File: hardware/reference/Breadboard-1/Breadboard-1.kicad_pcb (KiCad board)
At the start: 2 copper layers, 50.8 x 69.9 mm, 60 parts, among them J1 Left, J2 Right, J3 ICSP, J4 TTL Serial, Q31 HSM0903, Q32 HSM0903, Q41 2N7002, Q42 2N7002, Q43 2N7002, U11 AMS1117-5.0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

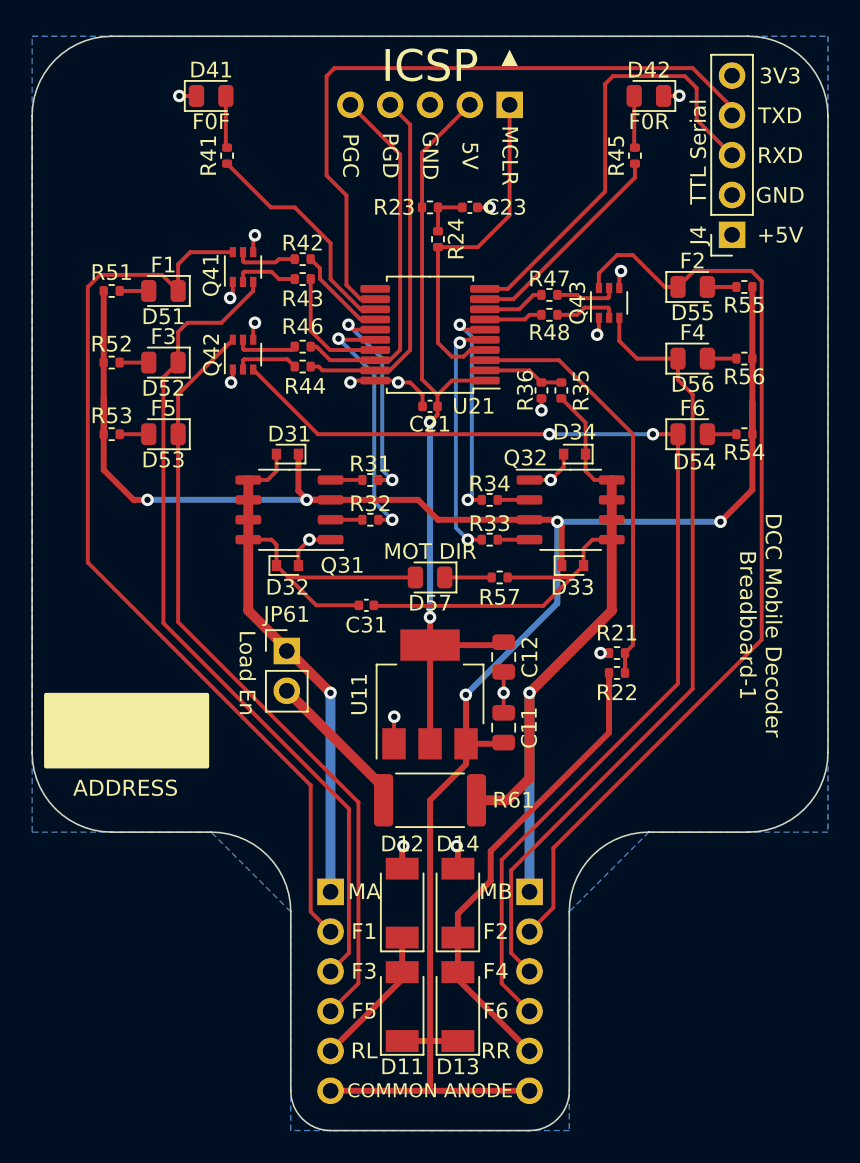
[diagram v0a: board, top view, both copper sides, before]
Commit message: Add pre-biased transistors to drive high side.  Update LED part to more common.
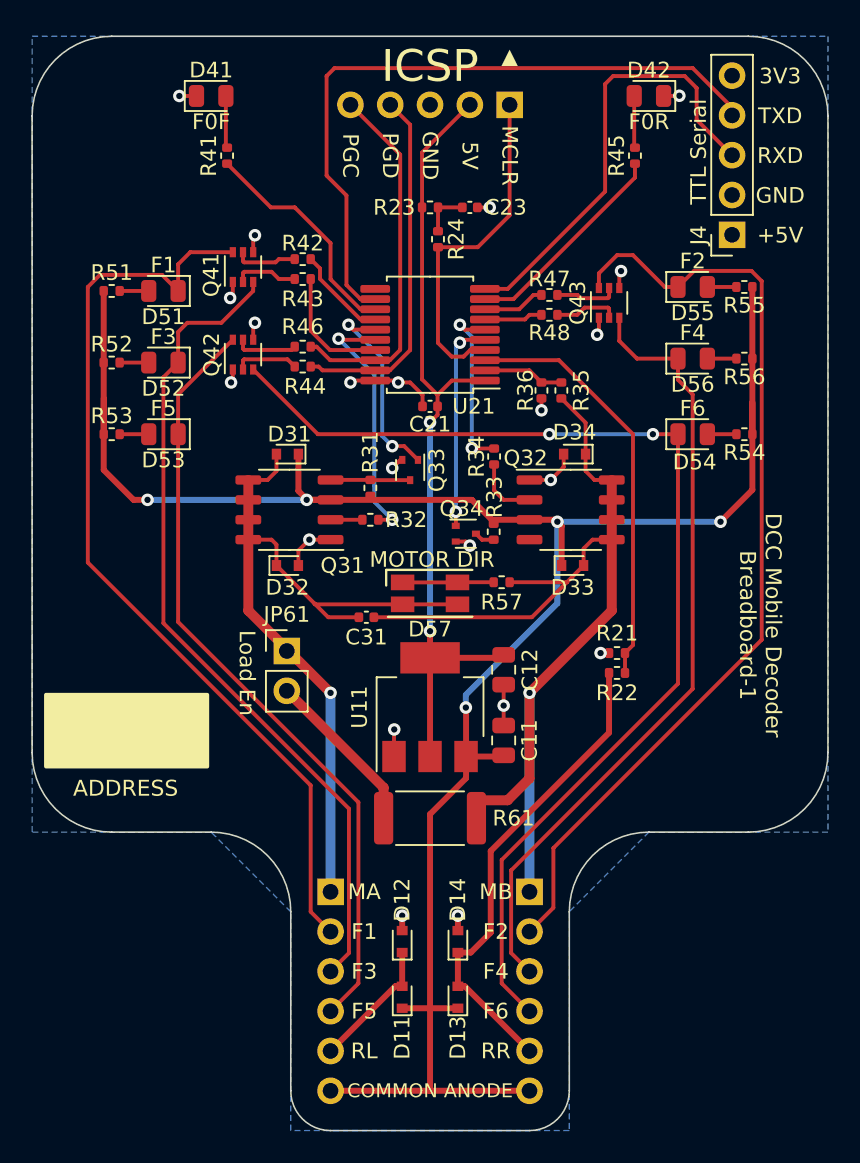
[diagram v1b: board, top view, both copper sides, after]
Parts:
- added Q33: DTC143ZE, Package_TO_SOT_SMD:SOT-523, F.Cu at (74.9, 78.5)
- added Q34: DTC143ZE, Package_TO_SOT_SMD:SOT-523, F.Cu at (78.5, 82.5)
- D11, D12, D13, D14: footprint Diode_SMD:D_SOD-128 -> Diode_SMD:D_SOD-523
- D57: value MOT DIR -> MOTOR DIR; footprint LED_SMD:LED_0805_2012Metric -> LED_SMD:LED_RGB_1210
- R31, R33: value 220 -> 10K
- moved R34 2.78 mm to (80.3, 77.6), turned to 90 degrees
- moved D12 2.45 mm to (74.4, 108.6)
- moved D14 2.45 mm to (78.0, 108.6)
- moved R61 1.14 mm to (76.2, 100.7)
- moved D57 1.02 mm to (76.2, 86.4), turned to 0 degrees
- moved C11 0.81 mm to (80.9, 95.7)
- moved C12 0.81 mm to (80.9, 91.2)
- moved U11 0.81 mm to (76.2, 93.6)
- moved C31 0.76 mm to (72.1, 87.9)
- moved D11 0.59 mm to (74.4, 112.1)
- moved D13 0.59 mm to (78.0, 112.1)
- moved R33 0.57 mm to (80.3, 82.4), turned to 90 degrees
- moved R31 0.51 mm to (72.4, 79.6), turned to -90 degrees
- moved R57 0.33 mm to (80.8, 85.6)
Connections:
- R31 pad 1: P1A -> Net-(Q31-Pad4)
- R31 pad 2: Net-(Q31-Pad4) -> Vdrive
- R33 pad 2: P1C -> Vdrive
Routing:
- net Net-(Q31-Pad4): track 2.03 -> 5.09 mm
- net P1D: track 14.2 -> 11.3 mm
- net Net-(D57-Pad1): track 3.00 -> 5.82 mm
- net Net-(Q32-Pad2): track 2.03 -> 4.16 mm
- net P1C: track 15.6 -> 13.5 mm
- net MOT_A: track 49.3 -> 50.6 mm
- net Net-(JP61-Pad2): track 9.55 -> 10.7 mm
- net GND: track 30.4 -> 31.4 mm, vias 19 -> 21
- net P1A: track 13.8 -> 12.7 mm
- net +5V: track 50.8 -> 51.6 mm
- net RAIL_R: track 30.4 -> 31.1 mm
- net Net-(Q32-Pad4): track 2.03 -> 1.29 mm
- net RAIL_L: track 9.46 -> 8.77 mm

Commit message: Attempt to refactor with all SOT-23 components for cost, availability.
Also makes it more possible to hand-solder.
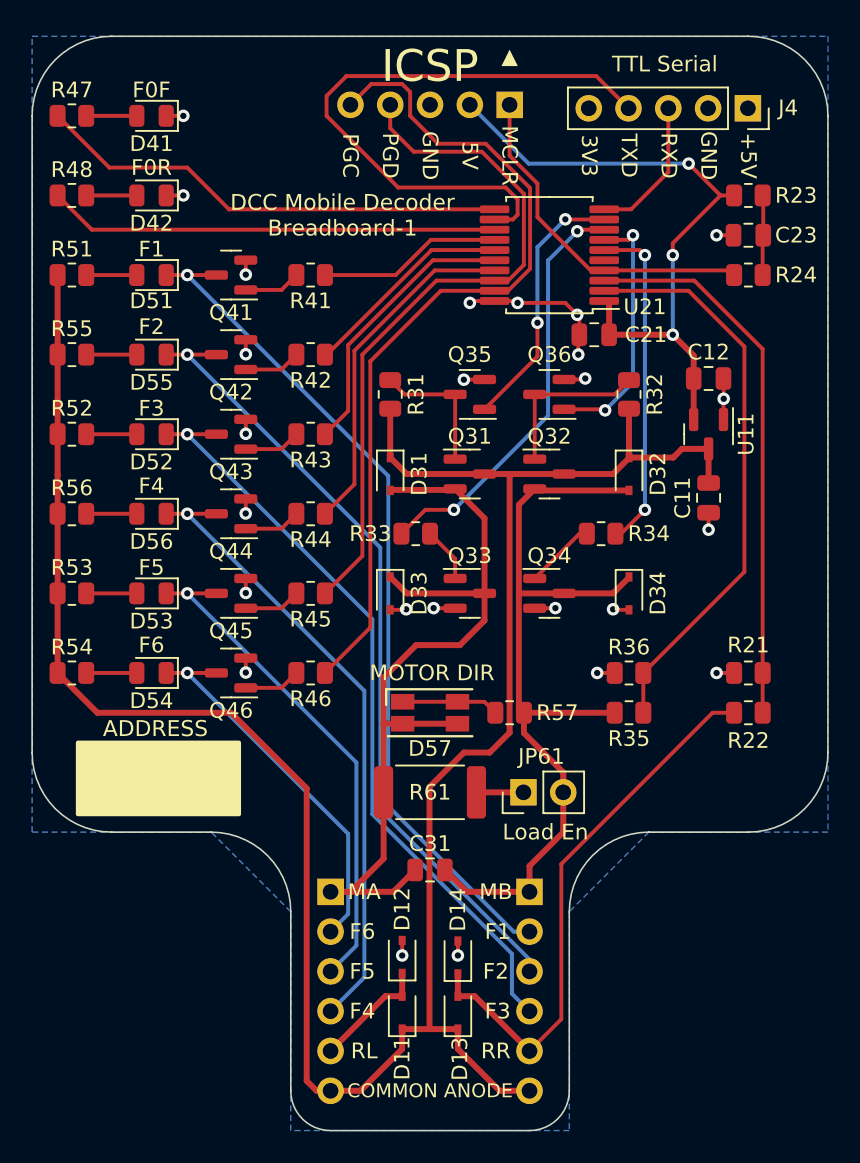
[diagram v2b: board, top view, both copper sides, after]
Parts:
- added Q33: DMN6140L-7, Package_TO_SOT_SMD:SOT-23, F.Cu at (78.7, 86.4)
- added Q34: DMN6140L-7, Package_TO_SOT_SMD:SOT-23, F.Cu at (83.8, 86.4)
- added Q44: 2N7002K, Package_TO_SOT_SMD:SOT-23, F.Cu at (63.5, 81.3)
- added Q45: 2N7002K, Package_TO_SOT_SMD:SOT-23, F.Cu at (63.5, 86.4)
- added Q46: 2N7002K, Package_TO_SOT_SMD:SOT-23, F.Cu at (63.5, 91.4)
- C21, C23, C31: footprint Capacitor_SMD:C_0402_1005Metric -> Capacitor_SMD:C_0805_2012Metric
- D11, D12, D13, D14, D31, D34: footprint Diode_SMD:D_SOD-523 -> Diode_SMD:D_SOD-323
- D32: renamed from D33; footprint Diode_SMD:D_SOD-523 -> Diode_SMD:D_SOD-323
- D33: renamed from D32; footprint Diode_SMD:D_SOD-523 -> Diode_SMD:D_SOD-323
- Q31, Q32: value HSM0903 -> NCE2309; footprint Package_SO:SOP-8_3.9x4.9mm_P1.27mm -> Package_TO_SOT_SMD:SOT-23
- Q35: renamed from Q33; value DTC143ZE -> DTC143ZCA; footprint Package_TO_SOT_SMD:SOT-523 -> Package_TO_SOT_SMD:SOT-23
- Q36: renamed from Q34; value DTC143ZE -> DTC143ZCA; footprint Package_TO_SOT_SMD:SOT-523 -> Package_TO_SOT_SMD:SOT-23
- Q41, Q42, Q43: value 2N7002 -> 2N7002K; footprint Package_TO_SOT_SMD:SOT-363_SC-70-6 -> Package_TO_SOT_SMD:SOT-23
- R21, R22, R23, R24, R31, R34, R35, R36, R43, R46, R51, R52, R53, R54, R55, R56, R57: footprint Resistor_SMD:R_0402_1005Metric -> Resistor_SMD:R_0805_2012Metric
- R32: renamed from R33; footprint Resistor_SMD:R_0402_1005Metric -> Resistor_SMD:R_0805_2012Metric
- R33: renamed from R32; footprint Resistor_SMD:R_0402_1005Metric -> Resistor_SMD:R_0805_2012Metric
- R41: renamed from R42; footprint Resistor_SMD:R_0402_1005Metric -> Resistor_SMD:R_0805_2012Metric
- R42: renamed from R47; footprint Resistor_SMD:R_0402_1005Metric -> Resistor_SMD:R_0805_2012Metric
- R44: renamed from R48; footprint Resistor_SMD:R_0402_1005Metric -> Resistor_SMD:R_0805_2012Metric
- R45: renamed from R44; footprint Resistor_SMD:R_0402_1005Metric -> Resistor_SMD:R_0805_2012Metric
- R47: renamed from R41; footprint Resistor_SMD:R_0402_1005Metric -> Resistor_SMD:R_0805_2012Metric
- R48: renamed from R45; footprint Resistor_SMD:R_0402_1005Metric -> Resistor_SMD:R_0805_2012Metric
- U11: value AMS1117-5.0 -> ME6203A50M3G; footprint Package_TO_SOT_SMD:SOT-223-3_TabPin2 -> Package_TO_SOT_SMD:SOT-23
- moved R54 45.6 mm to (53.3, 91.4), turned to 0 degrees
- moved R56 44.1 mm to (53.3, 81.3), turned to 0 degrees
- moved R55 43.1 mm to (53.3, 71.1), turned to 0 degrees
- moved D54 37.8 mm to (58.4, 91.4), turned to 180 degrees
- moved R48 36.0 mm to (53.3, 61.0), turned to 0 degrees
- moved D56 35.9 mm to (58.4, 81.3), turned to 180 degrees
- moved D55 34.8 mm to (58.4, 71.1), turned to 180 degrees
- moved D42 32.4 mm to (58.4, 61.0)
- moved Q43 25.5 mm to (63.5, 76.2), turned to 180 degrees
- moved U11 24.9 mm to (94.0, 76.2), turned to -90 degrees
- moved C12 22.7 mm to (94.0, 72.6), turned to 0 degrees
- moved R35 21.0 mm to (88.9, 94.0), turned to 180 degrees
- moved R46 20.8 mm to (68.6, 91.4)
- moved R44 20.7 mm to (68.6, 81.3), turned to 180 degrees
- moved R23 20.3 mm to (96.5, 61.0)
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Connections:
- J1 pad 2: F1_SP -> F6_SP
- J1 pad 3: F3_SP -> F5_SP
- J1 pad 4: F5_SP -> F4_SP
- J2 pad 2: F2_SP -> F1_SP
- J2 pad 3: F4_SP -> F2_SP
- J2 pad 4: F6_SP -> F3_SP
- JP61 pad 1: MOT_A -> Net-(JP61-Pad1)
- JP61 pad 2: Net-(JP61-Pad2) -> MOT_B
- Q31 pad 1: GND -> Net-(Q31-Pad1)
- Q31 pad 2: Net-(Q31-Pad2) -> MOT_A
- Q32 pad 1: GND -> Net-(Q32-Pad1)
- Q32 pad 2: Net-(Q32-Pad2) -> MOT_B
- Q35 pad 3: Net-(Q31-Pad4) -> Net-(Q31-Pad1)
- Q36 pad 3: Net-(Q32-Pad4) -> Net-(Q32-Pad1)
- Q41 pad 1: GND -> Net-(Q41-Pad1)
- Q41 pad 2: Net-(Q41-Pad2) -> GND
- Q41 pad 3: F3_SP -> F1_SP
- Q42 pad 1: GND -> Net-(Q42-Pad1)
- Q42 pad 2: Net-(Q42-Pad2) -> GND
- Q42 pad 3: F6_SP -> F2_SP
- Q43 pad 1: GND -> Net-(Q43-Pad1)
- Q43 pad 2: Net-(Q43-Pad2) -> GND
- Q43 pad 3: F4_SP -> F3_SP
- R31 pad 1: Net-(Q31-Pad4) -> Net-(Q31-Pad1)
- R32 pad 1: Net-(Q32-Pad4) -> Net-(Q32-Pad1)
- R33 pad 2: Net-(Q31-Pad2) -> Net-(Q33-Pad1)
- R34 pad 1: Net-(Q32-Pad2) -> Net-(Q34-Pad1)
- R41 pad 2: Net-(Q41-Pad2) -> Net-(Q41-Pad1)
- R42 pad 2: Net-(Q43-Pad2) -> Net-(Q42-Pad1)
- R43 pad 2: Net-(Q41-Pad5) -> Net-(Q43-Pad1)
- R44 pad 2: Net-(Q43-Pad5) -> Net-(Q44-Pad1)
- R45 pad 2: Net-(Q42-Pad2) -> Net-(Q45-Pad1)
- R46 pad 2: Net-(Q42-Pad5) -> Net-(Q46-Pad1)
- R61 pad 1: Net-(JP61-Pad2) -> MOT_A
- R61 pad 2: MOT_B -> Net-(JP61-Pad1)
- U21 pad 11: unconnected-(U21-Pad11) -> F0F
- U21 pad 13: F0F -> F0R
- U21 pad 14: F3 -> F1
- U21 pad 15: P1A -> F2
- U21 pad 16: P1B -> F3
- U21 pad 17: F1 -> F4
- U21 pad 18: PGC/F6 -> PGD/F5
- U21 pad 19: PGD/F5 -> PGC/F6
- U21 pad 5: P1C -> unconnected-(U21-Pad5)
- U21 pad 7: F2 -> P1C
- U21 pad 8: F4 -> P1B
- U21 pad 9: F0R -> P1A
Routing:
- net F6_SP: track 71.1 -> 24.4 mm, vias 2 -> 1
- net BackEMF: track 5.20 -> 36.5 mm
- net PGC/F6: track 23.3 -> 54.6 mm
- net PGD/F5: track 23.2 -> 45.1 mm
- net TXD: track 28.7 -> 9.14 mm
- net F4: track 3.99 -> 22.3 mm
- net F5_SP: track 50.7 -> 32.5 mm, vias 0 -> 1
- net F0F: track 14.7 -> 30.4 mm
- net F0R: track 13.7 -> 28.8 mm
- net MOT_B: track 66.6 -> 53.6 mm, vias 1 -> 0
- net P1B: track 16.2 -> 28.2 mm
- net F3: track 6.10 -> 17.9 mm
- net Vdrive: track 139.9 -> 150.7 mm, vias 5 -> 0
- net Net-(JP61-Pad2): track 10.7 -> 0.00 mm
- net Net-(Q32-Pad1): track 0.00 -> 10.5 mm
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
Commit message: Cleanup of the final PCB.
Moved components to grid coordinates.
Added in some labels for the user.
Cleaned up some trace routing, and made it pretty where possible.
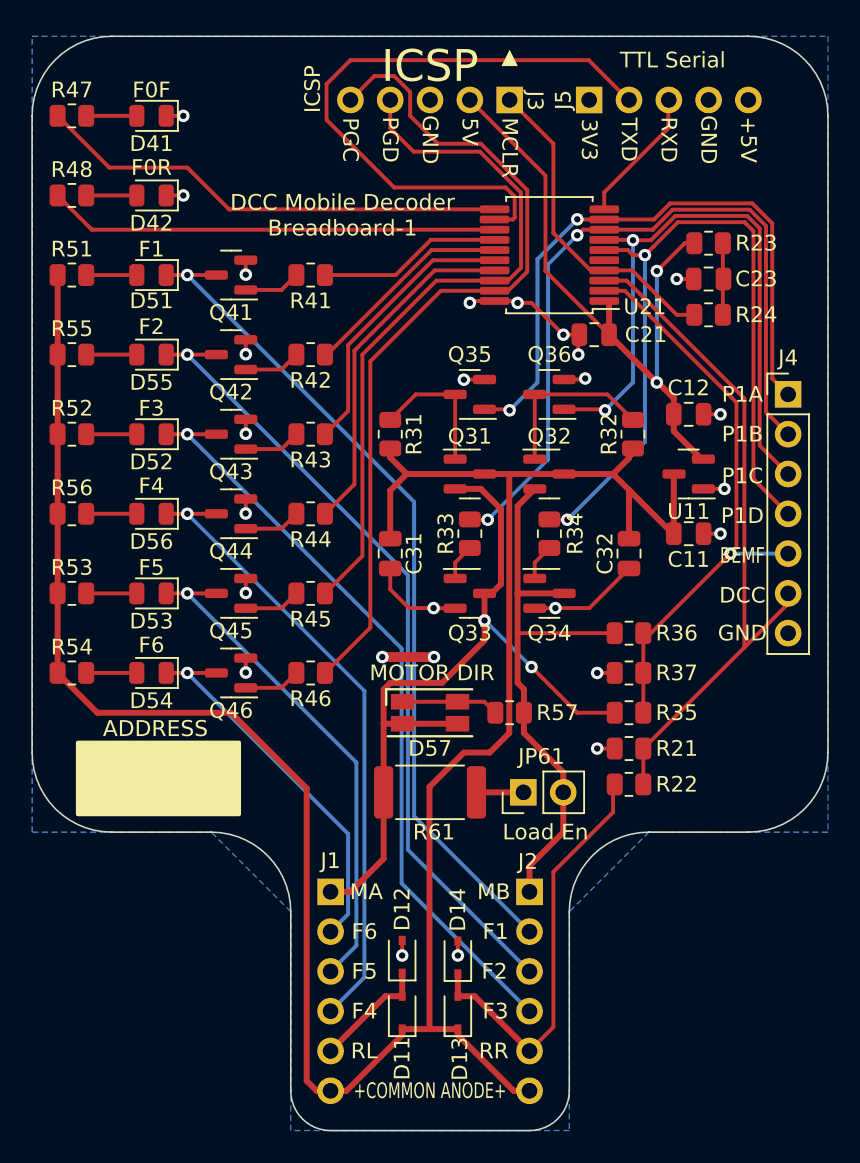
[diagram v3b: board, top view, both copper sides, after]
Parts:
- removed D31, D32, D33, D34: D_S, Diode_SMD:D_SOD-323
- added C32: 1uF, Capacitor_SMD:C_0805_2012Metric, F.Cu at (88.9, 83.8)
- added J4: Oscilloscope, Connector_PinHeader_2.54mm:PinHeader_1x07_P2.54mm_Vertical, F.Cu at (99.1, 73.7)
- added R36: 6K6, Resistor_SMD:R_0805_2012Metric, F.Cu at (88.9, 88.9)
- D11, D12, D13, D14: value D_S -> B5819WS
- J5: renamed from J4; footprint Connector_PinSocket_2.54mm:PinSocket_1x05_P2.54mm_Vertical -> Connector_PinSocket_2.54mm:PinSocket_1x05_P2.54mm_Horizontal; moved to B.Cu
- Q33, Q34: value DMN6140L-7 -> DMN6140L-7
- U21: value PIC18F06Q40-x/SS -> PIC18F16Q40-I/SS
- moved C31 20.4 mm to (73.7, 83.8), turned to 90 degrees
- moved J5 10.1 mm to (86.4, 54.9)
- moved R21 9.02 mm to (88.9, 96.3)
- moved R22 8.89 mm to (88.9, 98.6)
- moved R23 3.97 mm to (94.0, 64.0)
- moved C23 3.78 mm to (94.0, 66.3)
- moved R24 3.59 mm to (94.0, 68.6)
- moved R33 3.45 mm to (78.7, 82.5), turned to -90 degrees
- moved R34 3.30 mm to (83.8, 82.5), turned to 90 degrees
- moved U11 2.84 mm to (92.7, 78.7), turned to 180 degrees
- moved C11 2.62 mm to (92.7, 82.5), turned to 0 degrees
- moved C12 2.62 mm to (92.7, 74.9)
- moved R32 2.55 mm to (89.2, 76.2)
- moved R31 2.54 mm to (73.7, 76.2)
- moved J3 0.31 mm to (81.3, 54.9)
- renumbered R36 to R37
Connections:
- net Net-(R21-Pad1) renamed DCC_IN
- C31 pad 1: MOT_A -> GND
- C31 pad 2: MOT_B -> Vdrive
- J5 pad 2: GND -> RXD
- J5 pad 4: RXD -> GND
- R35 pad 2: MOT_B -> MOT_A
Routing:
- net P1D: track 21.5 -> 49.8 mm
- net P1C: track 16.5 -> 41.6 mm
- net P1A: track 16.8 -> 40.4 mm
- net P1B: track 28.2 -> 50.2 mm
- net MOT_B: track 53.6 -> 37.4 mm
- net GND: track 33.9 -> 44.6 mm, vias 25 -> 26
- net DCC_IN: track 35.1 -> 44.0 mm
- net RAIL_R: track 35.3 -> 26.7 mm
- net MOT_A: track 54.3 -> 50.8 mm, vias 0 -> 2
- net Vdrive: track 150.7 -> 153.9 mm
- net Net-(Q34-Pad1): track 4.51 -> 2.37 mm
- net Net-(Q33-Pad1): track 3.52 -> 2.34 mm
- net MCLR: track 22.0 -> 20.8 mm
- net BackEMF: track 36.5 -> 37.6 mm, vias 0 -> 1
- net RXD: track 38.9 -> 40.0 mm
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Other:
- board text added: "+COMMON ANODE+"
- board text added: "BEMF"
- board text added: "DCC"
- board text added: "P1A"
- board text added: "P1B"
- board text added: "P1C"
- board text added: "P1D"
- board text removed: "COMMON ANODE"

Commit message: Generated updated .JPG and .PDF for documentation.
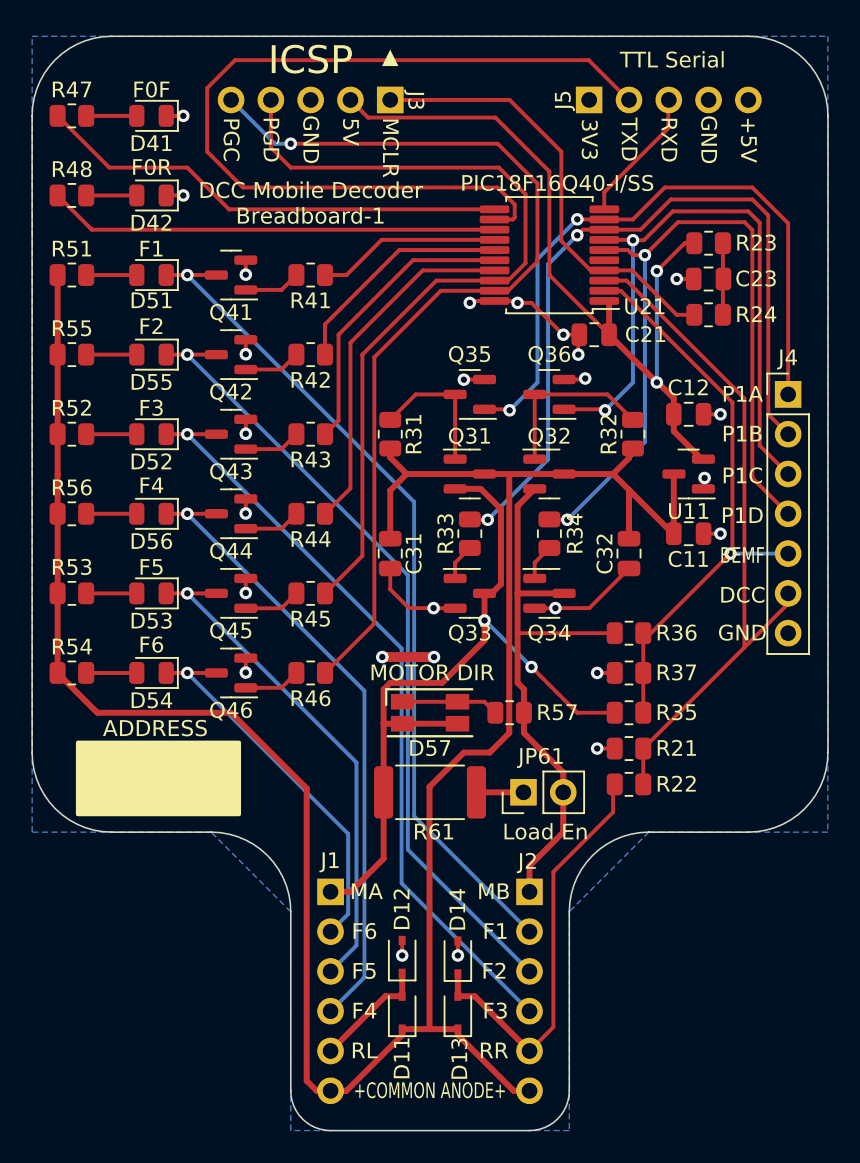
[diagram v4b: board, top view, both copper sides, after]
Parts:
- moved J3 7.62 mm to (73.7, 54.9)
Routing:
- net RXD: track 40.0 -> 55.9 mm
- net PGD/F5: track 45.2 -> 53.9 mm
- net +5V: track 41.6 -> 49.5 mm
- net MCLR: track 20.8 -> 28.4 mm
- net PGC/F6: track 54.5 -> 61.1 mm, vias 0 -> 1
- net P1A: track 40.4 -> 41.8 mm
- net F2: track 13.6 -> 14.7 mm
- net P1B: track 50.2 -> 51.2 mm
- net F3: track 17.9 -> 18.6 mm
- net GND: track 44.6 -> 44.0 mm
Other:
- board text removed: "ICSP"

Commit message: Minor design tweak, update documentation.
Moved the MCLEAR hold up components to make the board design cleaner.

Updated all the documentation to match the current configuration.
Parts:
- moved R23 18.7 mm to (77.7, 54.8), turned to -90 degrees
- moved C23 18.1 mm to (80.0, 54.8), turned to -90 degrees
- moved R24 18.1 mm to (82.3, 54.8), turned to -90 degrees
- moved J4 7.62 mm to (99.1, 66.0)
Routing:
- net RXD: track 55.9 -> 12.0 mm, vias 0 -> 1
- net P1D: track 49.8 -> 35.7 mm
- net P1C: track 42.0 -> 29.0 mm
- net P1B: track 51.2 -> 39.0 mm
- net P1A: track 41.8 -> 30.5 mm
- net MCLR: track 28.4 -> 22.1 mm
- net +5V: track 49.5 -> 46.3 mm, vias 2 -> 0
- net DCC_IN: track 44.0 -> 42.2 mm
- net Net-(C23-Pad2): track 4.60 -> 5.36 mm
